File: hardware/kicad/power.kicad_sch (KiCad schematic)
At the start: 5 parts, among them J1 Phoenix_MSTBA_2,5/3-G-5,08, Q1 AO3415A

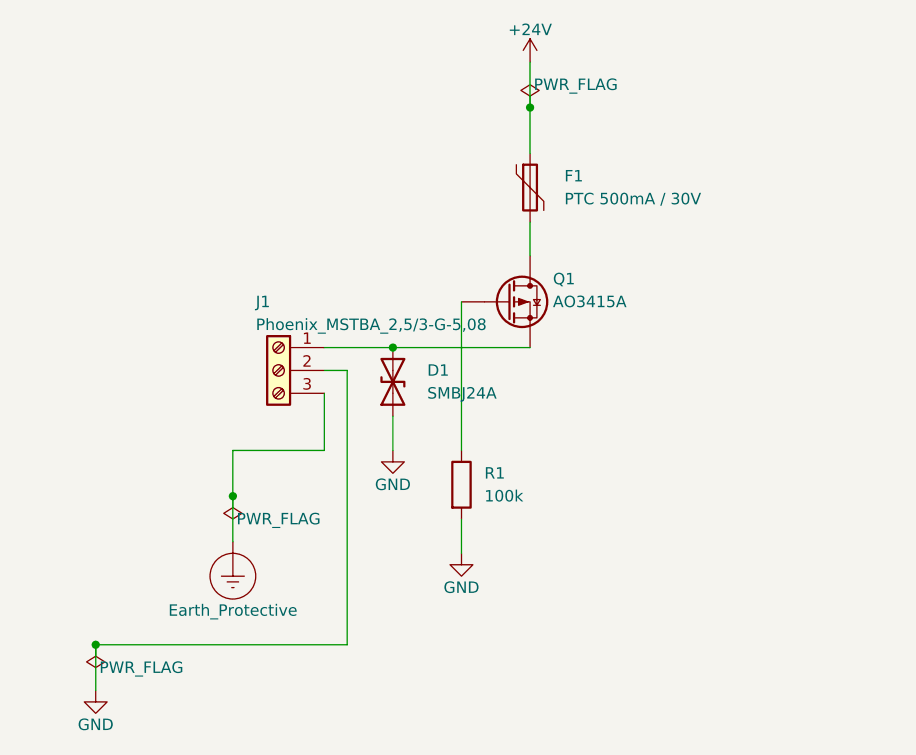
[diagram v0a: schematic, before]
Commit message: kicad: bulk cap C1 + Y-cap C2 (close power input section)
Adds the final two components of the 24V input protection
chain:

C1 (100uF 50V electrolytic) sits across the protected +24V
rail to GND, downstream of F1. Buffers transient load steps
from the WS2812 LED, mmWave radar refreshes, MCU TX bursts,
and absorbs ripple from the upstream supply. 50V rating
gives margin over both the 24V nominal and the SMBJ24A's
38.9V surge-clamping voltage.

C2 (10nF Y2 ceramic) sits between circuit GND and the PE
conductor (Earth_Protective net from J1 pin 3). Closes the
conducted-EMI loop so high-frequency switching noise from
the downstream bucks returns to chassis ground through this
cap rather than escaping along the supply leads. Y2 class
is mandatory for any GND-to-PE cap - it's rated for impulse
withstand and fails open-circuit (not short, which would
defeat the protective earth function).

Power input section is now complete: J1 -> D1 (TVS clamp)
-> Q1 (reverse-polarity PMOS) -> F1 (PTC fuse) -> C1 (bulk)
-> +24V rail. C2 sits independently across GND/PE for EMI.

ERC passes 0/0. Generation deterministic.

Co-Authored-By: Claude Opus 4.7 (1M context) <noreply@anthropic.com>
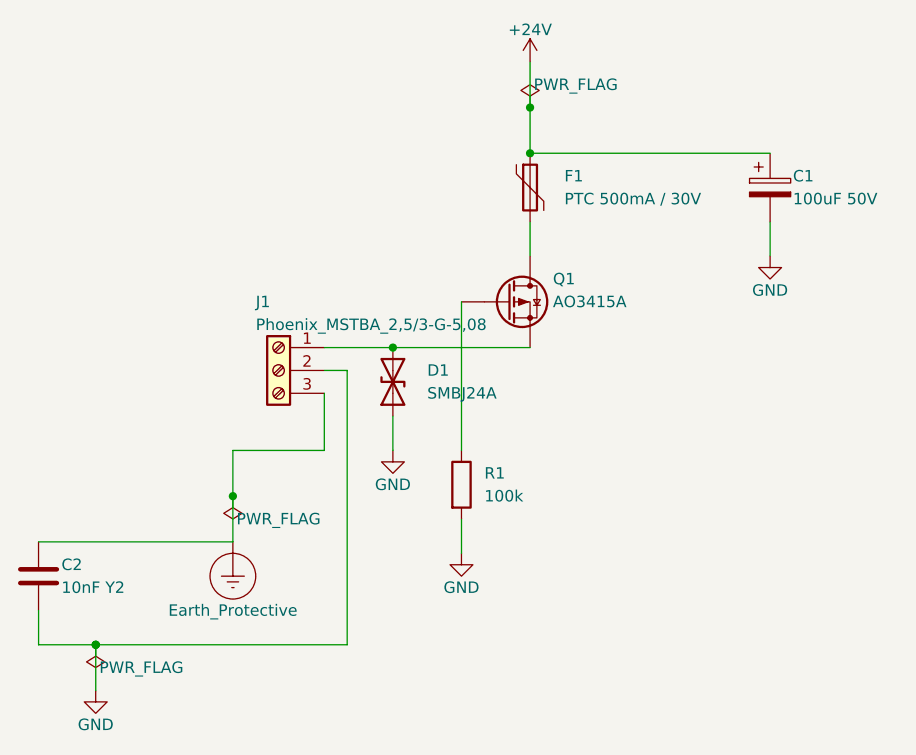
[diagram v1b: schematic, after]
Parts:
- added C1: 100uF 50V, symbol Device:C_Polarized
- added C2: 10nF Y2, symbol Device:C
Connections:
- net +24V: now also C1.1
- net Earth_Protective: now also C2.1
- net GND: now also C1.2, C2.2

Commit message: kicad: 24V to 5V buck converter (LM2596S-5.0, U1)
First active block: asynchronous step-down buck producing a
regulated 5V rail from the protected +24V input. Powers the
LD2410 mmWave radar and the WS2812 status LED.

Component selection rationale:
- LM2596S-5.0 (40V Vin_max, fixed 5V output, 3A, 150kHz,
  TO-263 DPAK): the 40V rating is critical because D1
  (SMBJ24A) clamps surges at 38.9V - lower-rated bucks
  (TPS62933, MP2451, MP1584) would die under those events.
  Fixed-output variant eliminates the FB divider and one
  potential source of layout error.
- L1: 33uH shielded inductor, 1A sat - sized per LM2596
  datasheet for 5V output at 150kHz with up to ~500mA load.
- D2: SS14 Schottky (40V/1A) - LM2596 is asynchronous so
  an external catch diode is mandatory.
- C3 100uF/50V + 100nF ceramic at input, C4 220uF/10V +
  100nF at output - standard buck input/output capacitor
  recommendations from the LM2596 datasheet.

ON/OFF pin tied to GND for always-on operation. Thermal
pad of U1 will need a copper pour to GND on the PCB
(handled later in PCB-layout chunk).

New +5V power rail with its own PWR_FLAG sentinel.

ERC passes 0/0. Generation deterministic.

Co-Authored-By: Claude Opus 4.7 (1M context) <noreply@anthropic.com>
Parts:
- added C3: 100uF 50V, symbol Device:C_Polarized
- added C3b, C4b: 100nF, symbol Device:C
- added C4: 220uF 10V, symbol Device:C_Polarized
- added D2: SS14, symbol Device:D_Schottky
- added L1: 33uH 1A, symbol Device:L
- added U1: LM2596S-5.0, Package_TO_SOT_SMD:TO-263-5_TabPin3, symbol Regulator_Switching:LM2596S-5
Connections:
- net +24V: now also C3.1, C3b.1, U1.1 (VIN)
- net GND: now also C3.2, C3b.2, C4.2, C4b.2, D2.2 (A), U1.3 (GND), U1.5 (~{ON}/OFF)
- new net: D2.1 (K), L1.2, U1.2 (OUT)
- new net +5V: C4.1, C4b.1, L1.1, U1.4 (FB)

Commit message: kicad: 5V to 3.3V buck converter (TPS62933, U2)
Second buck stage producing a regulated 3.3V rail from the
+5V output of U1 (LM2596). Powers the ESP32-C6 SuperMini
(via 3V3 pin direct, bypassing the module's internal LDO),
SEN66 air-quality sensor, VEML7700 ambient light sensor,
and the NT3H2211 NFC tag.

Component selection rationale:
- TPS62933 (17V Vin_max, 3A, synchronous, 500kHz, SOT-583
  adjustable): 17V is fine here because we cascade from
  +5V, not 24V. Synchronous topology eliminates the
  external Schottky catch diode required by LM2596,
  reducing BOM count and improving efficiency from ~80%
  to ~95% at our typical load.
- L2: 2.2uH per TPS62933 datasheet for 3.3V output at
  500kHz; shielded, 2A sat current.
- Feedback divider R2 (44.2k 1%) / R3 (10k 1%) sets
  Vout = 0.6 x (1 + R2/R3) = 3.25V, well within ESP32-C6's
  3.0-3.6V supply window. Divider draws ~60uA from rail.
- C5 10uF ceramic input + C5b 100nF, C6 22uF ceramic
  output + C6b 100nF - per TPS62933 datasheet
  recommendations. C7 100nF is the BST bootstrap cap
  between U2.BST and U2.SW (required by the high-side
  gate driver).

Cascade topology (24V -> 5V -> 3.3V) chosen over parallel
(separate 24V->3.3V buck) because:
- TPS62933 17V max rules out direct 24V input
- Better end-to-end efficiency than two LM2596 stages
- Synchronous + 500kHz needs much smaller inductor
- Smaller PCB area
- Cleaner BOM (single small SOT-583 part)

ESP32-C6 supplied via 3V3 pin direct (not 5V via VIN). This
bypasses the SuperMini module's onboard LDO, which would
dissipate ~250mW (5V->3.3V at 150mA), heating the board and
biasing nearby SEN66 temperature/humidity measurements
(OAS pillar #1: measurement quality).

EN pin tied directly to VIN (always-on). RT and SS pins
tied to GND for the default 500 kHz switching frequency
and default ~0.6 ms soft-start.

New +3.3V power rail with PWR_FLAG sentinel.

ERC passes 0/0. Generation deterministic.

Co-Authored-By: Claude Opus 4.7 (1M context) <noreply@anthropic.c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
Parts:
- added C5: 10uF 16V, symbol Device:C
- added C5b, C6b, C7: 100nF, symbol Device:C
- added C6: 22uF 10V, symbol Device:C
- added L2: 2.2uH 2A, symbol Device:L
- added R2: 44.2k 1%, symbol Device:R
- added R3: 10k 1%, symbol Device:R
- added U2: TPS62933, Package_TO_SOT_SMD:SOT-583-8, symbol Regulator_Switching:TPS62933
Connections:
- net +5V: now also C5.1, C5b.1, U2.2 (EN), U2.3 (VIN)
- net GND: now also C5.2, C5b.2, C6.2, C6b.2, R3.2, U2.1 (RT), U2.4 (GND), U2.7 (SS)
- new net: C7.2, L2.2, U2.5 (SW)
- new net: C7.1, U2.6 (BST)
- new net: R2.2, R3.1, U2.8 (FB)
- new net +3V3: C6.1, C6b.1, L2.1, R2.1

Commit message: kicad: post-review fixes - Q1 (DMP4015SK3) + F1 (60V PTC)
Addresses three findings from the schematic review run
after ab0893f:

BLOCKER fix: Q1 changed AO3415A -> DMP4015SK3. The original
AO3415A spec was misread - actual Vds_max is -20V and
Vgs_max is +/-8V (not -40V / +/-20V as previously
documented). At 24V input the part would be destroyed on
first power-up because Vgs = -24V exceeds the +/-8V
absolute maximum by 3x. DMP4015SK3 from Diodes
Incorporated provides Vds_max = -40V (margin over the
38.9V SMBJ24A surge clamp), Vgs_max = +/-20V (tolerates
the full 24V gate-source drive cleanly), Id_max = -5A,
RDS(on) ~70mOhm at Vgs=-10V, SOT-23-3 drop-in. JLCPCB
Extended Parts Library (acceptable for this project).

HIGH + MEDIUM fix: F1 changed MF-MSMF050 (500mA/30V) ->
MF-RHT075/60-2 (750mA/60V). The 30V rating of the
original part is exceeded by the SMBJ24A surge clamp at
38.9V (especially under a Q1-fail-short scenario), and the
500mA hold current was a marginal margin against C1
cold-start inrush. The MF-RHT075/60-2 provides 60V rating
(>50% margin over the surge clamp ceiling) and 750mA hold
(50% wider margin vs inrush peaks while staying within the
~350mA combined load budget). Same 1812 SMD package, still
PTC resettable, JLCPCB Basic Library.

Both fixes are pure value/text swaps - same KiCad symbols,
same footprints (to be assigned later), same topology, same
netlist. ERC and DRC unchanged at 0/0.

Generation deterministic.

Co-Authored-By: Claude Opus 4.7 (1M context) <noreply@anthropic.com>
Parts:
- F1: value PTC 500mA / 30V -> PTC 750mA / 60V
- Q1: value AO3415A -> DMP4015SK3
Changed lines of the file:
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@@
 		)
 	)
-	(property "Value" "AO3415A"
+	(property "Value" "DMP4015SK3"
 		(at 118.11 88.9 0)
 		(effects
@@
 		)
 	)
-	(property "Value" "PTC 500mA / 30V"
+	(property "Value" "PTC 750mA / 60V"
 		(at 119.38 77.47 0)
 		(effects
